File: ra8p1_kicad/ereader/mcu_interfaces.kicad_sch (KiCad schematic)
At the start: 9 parts, among them U1 R7KA8P1KFLCAC#UC0

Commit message: Add microSD socket and verified mechanical card detect
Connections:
- net SD_CD_N: now reaches U1.F14 (P406)
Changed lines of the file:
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@@
+	(wire
+		(pts
+			(xy 304.8 63.5) (xy 330.2 63.5)
+		)
+		(stroke
+			(width 0)
+			(type default)
+		)
+	)
 	(wire
 		(pts
@@
 		)
 	)
+	(hierarchical_label "SD_CD_N"
+		(shape input)
+		(at 304.8 63.5 180)
+		(effects
+			(font
+				(size 1.27 1.27)
+			)
+			(justify right)
+		)
+	)

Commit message: hardware: integrate supervised microSD power and SDHI bus (#827, #845, #846)
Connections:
- net SD_IO_REQ: now reaches U1.N12 (P708)
- net SD_PWR_REQ: now reaches U1.N6 (P106)
- net SD_DAT3: now reaches U1.G12 (P405)
- net SD_DAT1: now reaches U1.H13 (P403)
- net SD_DAT2: now reaches U1.J13 (P404)
- net SD_DAT0: now reaches U1.L14 (P402)
- net SD_CMD: now reaches U1.N17 (P401)
- net SD_CLK: now reaches U1.P17 (P400)
- net SD_READY: now reaches U1.R17 (P407)
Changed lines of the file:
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@@
+		)
+	)
+	(hierarchical_label "SD_IO_REQ"
+		(shape output)
+		(at 71.12 142.24 0)
+		(effects
+			(font
+				(size 1.27 1.27)
+			)
+			(justify left)
 		)
 	)
@@
 		)
 	)
+	(hierarchical_label "SD_CLK"
+		(shape output)
+		(at 330.2 48.26 180)
+		(effects
+			(font
+				(size 1.27 1.27)
+			)
+			(justify right)
+		)
+	)
+	(hierarchical_label "SD_DAT1"
+		(shape bidirectional)
+		(at 330.2 55.88 180)
+		(effects
+			(font
+				(size 1.27 1.27)
+			)
+			(justify right)
+		)
+	)
 	(hierarchical_label "SDRAM_RAS_N"
 		(shape output)
@@
 		)
 	)
+	(hierarchical_label "SD_DAT0"
+		(shape bidirectional)
+		(at 330.2 53.34 180)
+		(effects
+			(font
+				(size 1.27 1.27)
+			)
+			(justify right)
+		)
+	)
 	(hierarchical_label "SDRAM_CLK"
 		(shape output)
@@
 		)
 	)
+	(hierarchical_label "SD_CMD"
+		(shape bidirectional)
+		(at 330.2 50.8 180)
+		(effects
+			(font
+				(size 1.27 1.27)
+			)
+			(justify right)
+		)
+	)
 	(hierarchical_label "SD_CD_N"
 		(shape input)
@@
 		)
 	)
+	(hierarchical_label "SD_PWR_REQ"
+		(shape output)
+		(at 167.64 63.5 0)
+		(effects
+			(font
+				(size 1.27 1.27)
+			)
+			(justify left)
+		)
+	)
 	(hierarchical_label "PAGE_NEXT_N"
 		(shape input)
@@
 		(effects
 			(font
+				(size 1.27 1.27)
+			)
+			(justify right)
+		)
+	)
+	(hierarchical_label "SD_DAT3"
+		(shape bidirectional)
+		(at 330.2 60.96 180)
+		(effects
+			(font
+				(size 1.27 1.27)
+			)
+			(justify right)
+		)
+	)
+	(hierarchical_label "SD_DAT2"
+		(shape bidirectional)
+		(at 330.2 58.42 180)
+		(effects
+			(font
+				(size 1.27 1.27)
+			)
+			(justify right)
+		)
+	)
+	(hierarchical_label "SD_READY"
+		(shape input)
+		(at 330.2 66.04 180)
+		(effects
+			(font

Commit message: hardware: integrate MIPI host 1.8V supply and bypass (#824, #841)
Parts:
- added C111: 100n, symbol Device:C_Small
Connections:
- net GND: now also C111.2
- net +1V8_MIPI: now reaches U1.R2 (VCC18_MIPI)
- net +1V8_MIPI: now also C111.1
- no-connect marks 7 -> 6
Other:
- note added: "CMS-013: R2 VCC18_MIPI = +1V8_MIPI from U23. C111: 100 nF local bypass to VSS_MIPI/GND (RA8P1 QDG Rev.1.10, Table 1); C39 bypasses AVCC_MIPI. Camera lanes and operating sequence remain pending. Keep CSI/DSI stopped until integration is qualified."
- note removed: "MIPI unused: AVCC_MIPI to VCC; VSS_MIPI to GND. Leave VCC18_MIPI and all six D-PHY lanes open. Firmware: MSTPCRC.MSTPC10=1 and MSTPC17=1. RA8P1 HUM Rev.1.30, section 21.4, p.862."

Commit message: Integrate Pcam camera and reserve dual-camera MCU routes (#821)
Join CSI and camera control hierarchy, migrate the radio bus and volume-up input, and preserve the reviewed net partitions. Enlarge root and MCU pages and refresh the 13-page PDF and native BOM.

Record dual-camera lighting and wet-port requirements plus parallel-module qualification gaps. Native/CLI ERC: 121 errors and 2 warnings; full design remains incomplete. Independent connectivity review passed; version and whitespace checks passed. ASCII check retains the pre-existing 63-character PARTS-CHECKLIST failure. Hardware-only hook bypass authorized by the owner.
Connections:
- net RADIO_CIPO: now also U1.P2 (P602); no longer U1.F12 (P700)
- net RADIO_COPI: now also U1.P1 (P603); no longer U1.F15 (P701)
- net RADIO_CS_N: now also U1.N2 (P604); no longer U1.G14 (P703)
- net RADIO_SCLK: now also U1.P4 (P601); no longer U1.F13 (P702)
- net VOL_UP_N: now also U1.C11 (P307); no longer U1.B14 (P909)
- net CAM_PWR_REQ: now reaches U1.P16 (P709)
- net CAM_SCL: now reaches U1.P13 (P512)
- net CAM_SDA: now reaches U1.U15 (P511)
- net CAM_D0_P: now reaches U1.T1 (MIPI_DL0_P)
- net CAM_CLK_P: now reaches U1.T2 (MIPI_CL_P)
- net CAM_D1_P: now reaches U1.T3 (MIPI_DL1_P)
- net CAM_D0_N: now reaches U1.U1 (MIPI_DL0_N)
- net CAM_CLK_N: now reaches U1.U2 (MIPI_CL_N)
- net CAM_D1_N: now reaches U1.U3 (MIPI_DL1_N)
- no-connect marks 6 -> 0
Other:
- note added: "CMS-016: SCI0 SCK=P601; CIPO=P602; COPI=P603; CS_N=P604. READY=P704/IRQ26; HANDSHAKE=P705/IRQ19. P706=RESET_REQ_N; P707=PWR_EN. Host-domain signals. Timing, switched-domain isolation and reset arbitration remain open."
- note removed: "RADIO-008: SPIA_C P700..P703; IRQ26=P704, IRQ19=P705. P706=RESET_REQ_N; P707=PWR_EN. Host-domain signals. Switched-domain isolation and reset arbitration remain open. Pin map + conflicts: ../design/radio_interface.md#radio-008-ra8p1-host-allocation"
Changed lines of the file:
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@@
 	(generator "eeschema")
 	(generator_version "10.0")
-	(paper "A3")
+	(paper "A2")
 	(title_block
 		(title "RA8P1 IO allocation")
@@
 		)
 	)
-	(text "RADIO-008: SPIA_C P700..P703; IRQ26=P704, IRQ19=P705.\nP706=RESET_REQ_N; P707=PWR_EN. Host-domain signals.\nSwitched-domain isolation and reset arbitration remain open.\nPin map + conflicts: ../design/radio_interface.md#radio-008-ra8p1-host-allocation"
+	(text "CMS-016: SCI0 SCK=P601; CIPO=P602; COPI=P603; CS_N=P604.\nREADY=P704/IRQ26; HANDSHAKE=P705/IRQ19.\nP706=RESET_REQ_N; P707=PWR_EN. Host-domain signals.\nTiming, switched-domain isolation and reset arbitration remain open."
 		(exclude_from_sim no)
 		(at 42.926 165.1 0)
@@
 			)
 			(justify left top)
-			(href "https://github.com/bsikar/ra8-firmware/blob/design/ereader-circuit/ra8p1_kicad/design/radio_interface.md#radio-008-ra8p1-host-allocation")
+			(href "https://github.com/bsikar/ra8-firmware/blob/design/ereader-circuit/ra8p1_kicad/design/camera_storage_interfaces.md#cms-016-two-camera-expansion-and-lighting-requirements")
 		)
 	)
@@
 	(text "PWR-001: C39 AVCC_MIPI bypass, 100 nF (QDG Table 2, p.7).\nTDK C1608X7R1H104K080AA; also used at C6 and C16-C34.\nInitial C = 100*(1 +/-0.10) = 90..110 nF; 50 V X7R.\nTDK DC-bias samples: 99.5575 nF / 3.15 V; 98.9525 nF / 4 V.\nC(3.3 V) = 99.5575 + (3.3-3.15)/0.85*(-0.605) = 99.45 nF.\nInterpolated nominal reference, NOT a guaranteed minimum.\nFinal rail / PDN qualification open; 3.3/50*100 = 6.6% rating.\nFull basis + Python check: design/power_decoupling.md"
 		(exclude_from_sim no)
-		(at 88.9 261.62 0)
+		(at 33.782 282.448 0)
 		(effects
 			(font
-				(size 1.27 1.27)
+				(size 1.778 1.778)
 			)
+			(justify left)
 			(href "https://github.com/bsikar/ra8-firmware/blob/design/ereader-circuit/ra8p1_kicad/design/power_decoupling.md#pwr-001-c39-mipi-analog-supply-bypass")
 		)
@@
 		(color 0 0 0 0)
 	)
-	(no_connect
-		(at 81.28 205.74)
-	)
-	(no_connect
-		(at 81.28 198.12)
-	)
-	(no_connect
-		(at 81.28 203.2)
-	)
-	(no_connect
-		(at 81.28 210.82)
-	)
-	(no_connect
-		(at 81.28 208.28)
-	)
-	(no_connect
-		(at 81.28 200.66)
-	)
 	(wire
 		(pts
@@
 	(wire
 		(pts
+			(xy 360.68 76.2) (xy 368.3 76.2)
+		)
+		(stroke
+			(width 0)
+			(type default)
+		)
+	)
+	(wire
+		(pts
 			(xy 91.44 190.5) (xy 91.44 195.58)
 		)
@@
 	(wire
 		(pts
+			(xy 71.12 144.78) (xy 76.2 144.78)
+		)
+		(stroke
+			(width 0)
+			(type default)
+		)
+	)
+	(wire
+		(pts
 			(xy 233.68 160.02) (xy 233.68 170.18)
 		)
@@
 	(wire
 		(pts
-			(xy 167.64 139.7) (xy 182.88 139.7)
+			(xy 264.16 66.04) (xy 279.4 66.04)
 		)
 		(stroke
@@
 	(wire
 		(pts
-			(xy 71.12 124.46) (xy 96.52 124.46)
+			(xy 33.02 129.54) (xy 40.64 129.54)
 		)
 		(stroke
@@
 	(wire
 		(pts
+			(xy 81.28 198.12) (xy 85.09 198.12)
+		)
+		(stroke
+			(width 0)
+			(type default)
+		)
+	)
+	(wire
+		(pts
 			(xy 167.64 78.74) (xy 175.26 78.74)
 		)
@@
 	(wire
 		(pts
+			(xy 81.28 200.66) (xy 85.09 200.66)
+		)
+		(stroke
+			(width 0)
+			(type default)
+		)
+	)
+	(wire
+		(pts
 			(xy 360.68 68.58) (xy 368.3 68.58)
 		)
@@
 	(wire
 		(pts
+			(xy 81.28 208.28) (xy 85.09 208.28)
+		)
+		(stroke
+			(width 0)
+			(type default)
+		)
+	)
+	(wire
+		(pts
 			(xy 17.78 144.78) (xy 40.64 144.78)
 		)
@@
 	(wire
 		(pts
-			(xy 71.12 129.54) (xy 96.52 129.54)
+			(xy 33.02 132.08) (xy 40.64 132.08)
 		)
 		(stroke
@@
 	(wire
 		(pts
-			(xy 71.12 127) (xy 96.52 127)
+			(xy 33.02 124.46) (xy 40.64 124.46)
 		)
 		(stroke
@@
 	(wire
 		(pts
+			(xy 81.28 210.82) (xy 85.09 210.82)
+		)
+		(stroke
+			(width 0)
+			(type default)
+		)
+	)
+	(wire
+		(pts
 			(xy 307.34 149.86) (xy 330.2 149.86)
 		)
@@
 	(wire
 		(pts
+			(xy 360.68 78.74) (xy 368.3 78.74)
+		)
+		(stroke
+			(width 0)
+			(type default)
+		)
+	)
+	(wire
+		(pts
 			(xy 304.8 205.74) (xy 304.8 213.36)
 		)
@@
 	(wire
 		(pts
+			(xy 81.28 205.74) (xy 85.09 205.74)
+		)
+		(stroke
+			(width 0)
+			(type default)
+		)
+	)
+	(wire
+		(pts
 			(xy 264.16 73.66) (xy 279.4 73.66)
 		)
@@
 	(wire
 		(pts
-			(xy 71.12 121.92) (xy 96.52 121.92)
+			(xy 33.02 127) (xy 40.64 127)
 		)
 		(stroke
@@
 	(wire
 		(pts
+			(xy 81.28 203.2) (xy 85.09 203.2)
+		)
+		(stroke
+			(width 0)
+			(type default)
+		)
+	)
+	(wire
+		(pts
 			(xy 304.8 200.66) (xy 304.8 190.5)
 		)
@@
 		)
 	)
+	(hierarchical_label "CAM_CLK_N"
+		(shape input)
+		(at 85.09 198.12 0)
+		(effects
+			(font
+				(size 1.27 1.27)
+			)
+			(justify left)
+		)
+	)
+	(hierarchical_label "CAM_D0_P"
+		(shape input)
+		(at 85.09 205.74 0)
+		(effects
+			(font
+				(size 1.27 1.27)
+			)
+			(justify left)
+		)
+	)
 	(hierarchical_label "SDRAM_CS_N"
 		(shape output)
@@
 	(hierarchical_label "VOL_UP_N"
 		(shape input)
-		(at 182.88 139.7 0)
+		(at 279.4 66.04 0)
+		(effects
+			(font
+				(size 1.27 1.27)
+			)
+			(justify left)
+		)
+	)
+	(hierarchical_label "CAM_D1_N"
+		(shape input)
+		(at 85.09 208.28 0)
 		(effects
 			(font
@@
 		)
 	)
+	(hierarchical_label "CAM_D0_N"
+		(shape input)
+		(at 85.09 203.2 0)
+		(effects
+			(font
+				(size 1.27 1.27)
+			)
+			(justify left)
+		)
+	)
+	(hierarchical_label "CAM_PWR_REQ"
+		(shape output)
+		(at 76.2 144.78 0)
+		(effects
+			(font
+				(size 1.27 1.27)
+			)
+			(justify left)
+		)
+	)
 	(hierarchical_label "SD_CMD"
 		(shape bidirectional)
@@
 		)
 	)
+	(hierarchical_label "CAM_D1_P"
+		(shape input)
+		(at 85.09 210.82 0)
+		(effects
+			(font
+				(size 1.27 1.27)
+			)
+			(justify left)
+		)
+	)
 	(hierarchical_label "SDRAM_A[0..12]"
 		(shape output)
@@
 		)
 	)
+	(hierarchical_label "CAM_SDA"
+		(shape bidirectional)
+		(at 368.3 76.2 0)
+		(effects
+			(font
+				(size 1.27 1.27)
+			)
+			(justify left)
+		)
+	)
 	(hierarchical_label "VOL_DOWN_N"
 		(shape input)
@@
 	(hierarchical_label "RADIO_SCLK"
 		(shape output)
-		(at 96.52 127 0)
+		(at 33.02 124.46 180)
 		(effects
 			(font
 				(size 1.27 1.27)
 			)
-			(justify left)
+			(justify right)
 		)
 	)
@@
 	(hierarchical_label "RADIO_CIPO"
 		(shape input)
-		(at 96.52 121.92 0)
+		(at 33.02 127 180)
 		(effects
 			(font
 				(size 1.27 1.27)
 			)
-			(justify left)
+			(justify right)
 		)
 	)
 	(hierarchical_label "RADIO_COPI"
 		(shape output)
-		(at 96.52 124.46 0)
+		(at 33.02 129.54 180)
 		(effects
 			(font
 				(size 1.27 1.27)
 			)
-			(justify left)
+			(justify right)
 		)
 	)
@@
 	(hierarchical_label "RADIO_CS_N"
 		(shape output)
-		(at 96.52 129.54 0)
+		(at 33.02 132.08 180)
 		(effects
 			(font
 				(size 1.27 1.27)
 			)
-			(justify left)
+			(justify right)
 		)
 	)
@@
 		)
 	)
+	(hierarchical_label "CAM_SCL"
+		(shape bidirectional)
+		(at 368.3 78.74 0)
+		(effects
+			(font
+				(size 1.27 1.27)
+			)
+			(justify left)
+		)
+	)
+	(hierarchical_label "CAM_CLK_P"
+		(shape input)
+		(at 85.09 200.66 0)
+		(effects
+			(font
+				(size 1.27 1.27)
+			)
+			(justify left)
+		)
+	)
 	(hierarchical_label "PAGE_NEXT_N"
 		(shape input)
@@
 		)
 		(pin "C11"
+			(alternate "P307_IN")
 		)
 		(pin "C9"

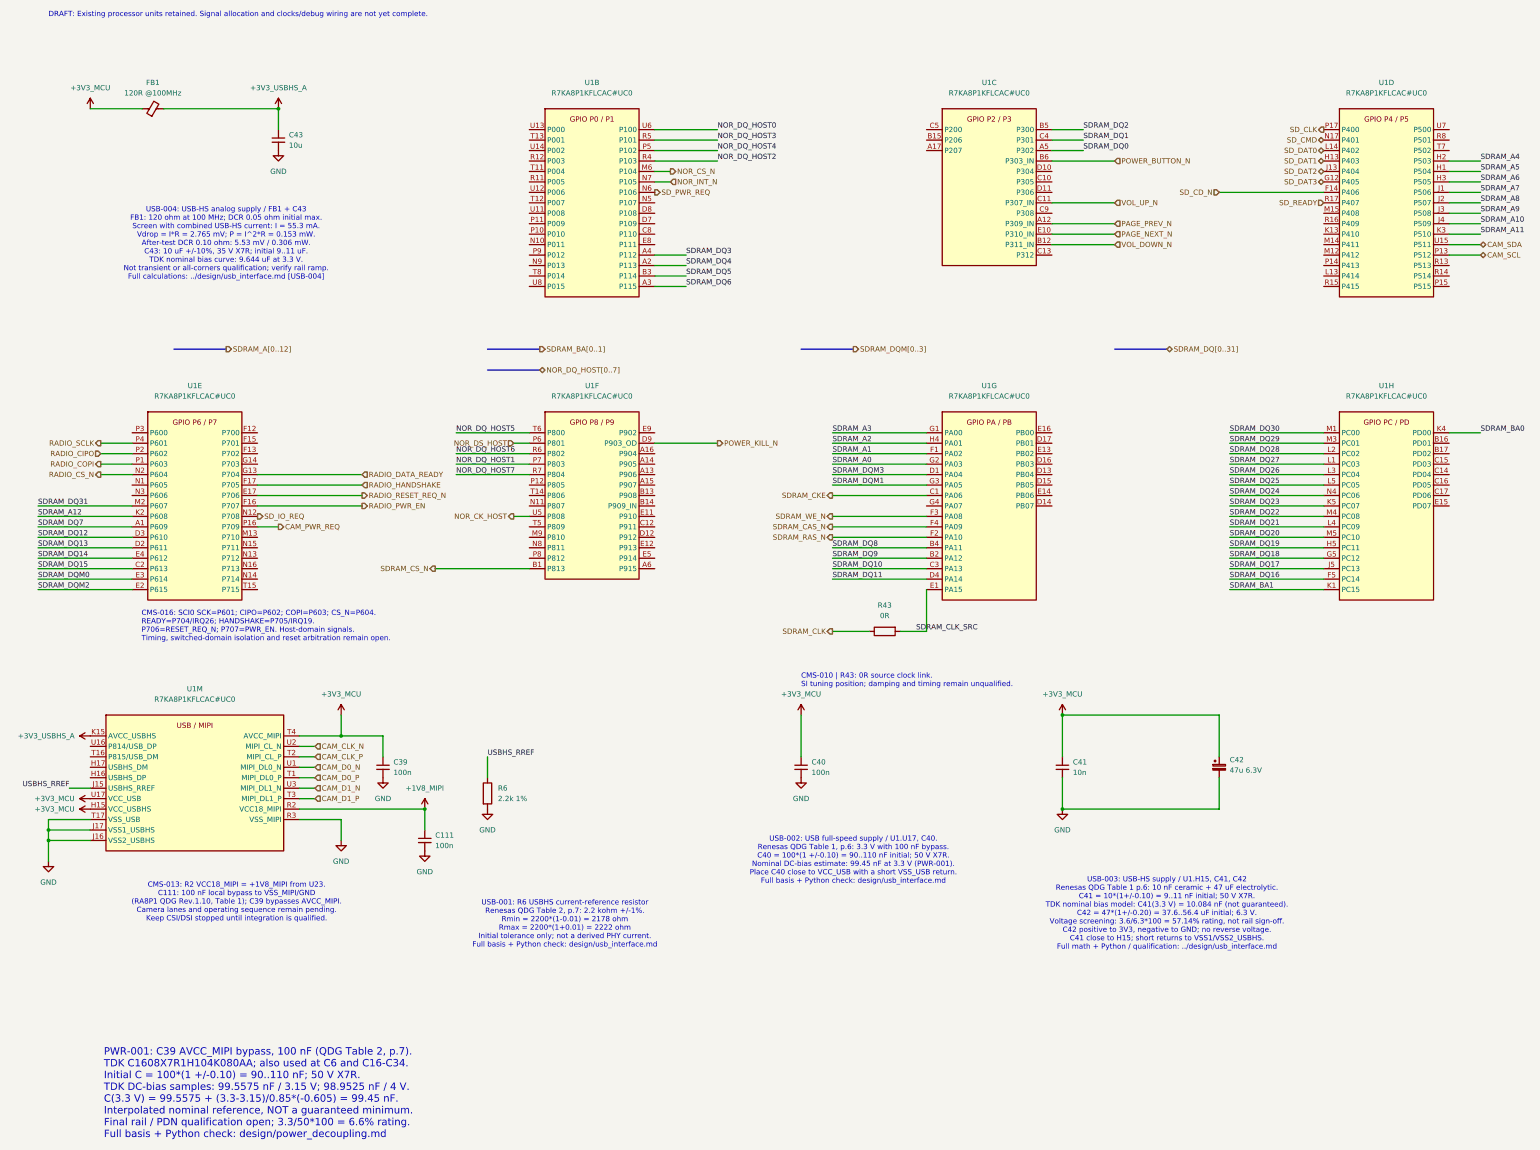
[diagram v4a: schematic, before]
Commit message: wip(hardware): preserve schematic cleanup and CEU host ports
Checkpoint cosmetic cleanup across the schematic hierarchy and eleven parallel-camera host ports. Refresh the complete 13-page PDF. All 334 existing net partitions and 271 component records match the prior CEU checkpoint; all 128 ERC identities remain unchanged. Electrical design is incomplete; this is a WIP checkpoint for #821 and #841.
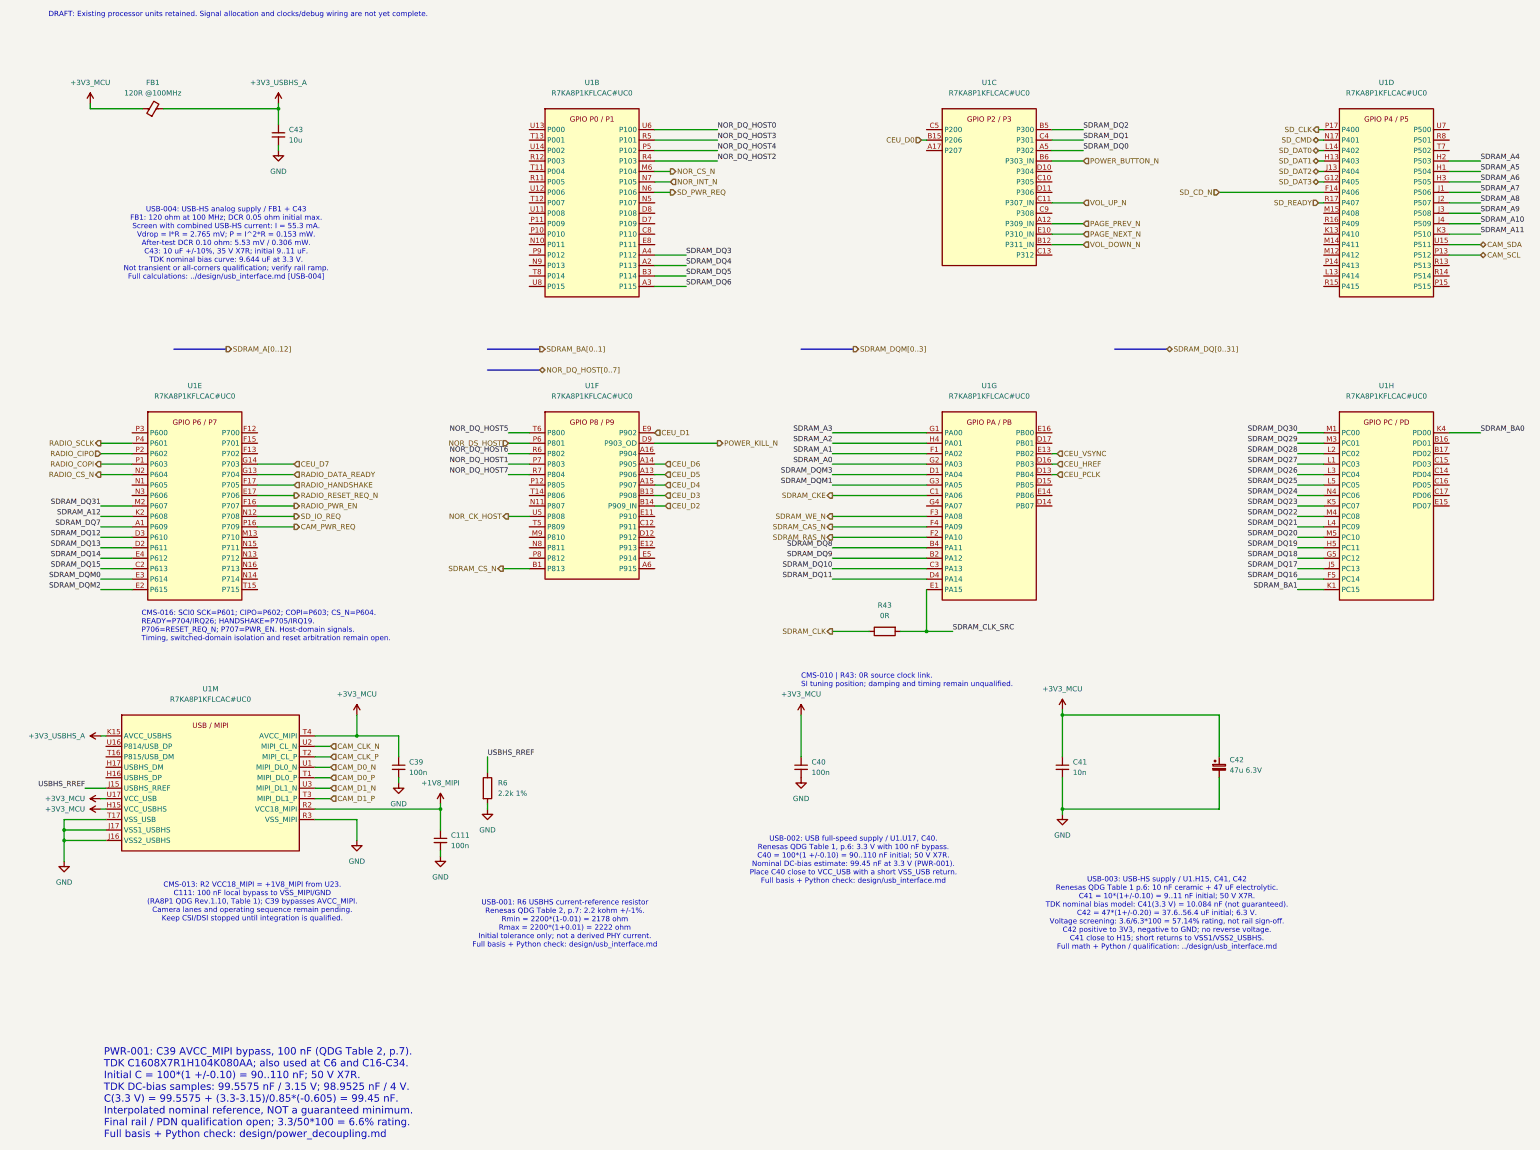
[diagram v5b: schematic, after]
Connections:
- net CEU_D7: now reaches U1.G14 (P703)
- net CEU_D0: now reaches U1.B15 (P206)
- net CEU_PCLK: now reaches U1.D13 (PB04)
- net CEU_HREF: now reaches U1.D16 (PB03)
- net CEU_VSYNC: now reaches U1.E13 (PB02)
- net CEU_D5: now reaches U1.A13 (P906)
- net CEU_D6: now reaches U1.A14 (P905)
- net CEU_D4: now reaches U1.A15 (P907)
- net CEU_D3: now reaches U1.B13 (P908)
- net CEU_D2: now reaches U1.B14 (P909)
- net CEU_D1: now reaches U1.E9 (P902)
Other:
- moved on the sheet: C111, C39, C43, R6, U1M
